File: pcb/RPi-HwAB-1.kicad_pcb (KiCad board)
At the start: 2 copper layers, 65 x 56 mm, 13 parts, among them J1 GPIO, J2 Hirose_FH12-16S, J3 TC2030, J4 Conn_ARM_SWD_TagConnect_TC203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, U1 XC7A35T-FGG484, U2 CAT24C256, U3 ADP5054

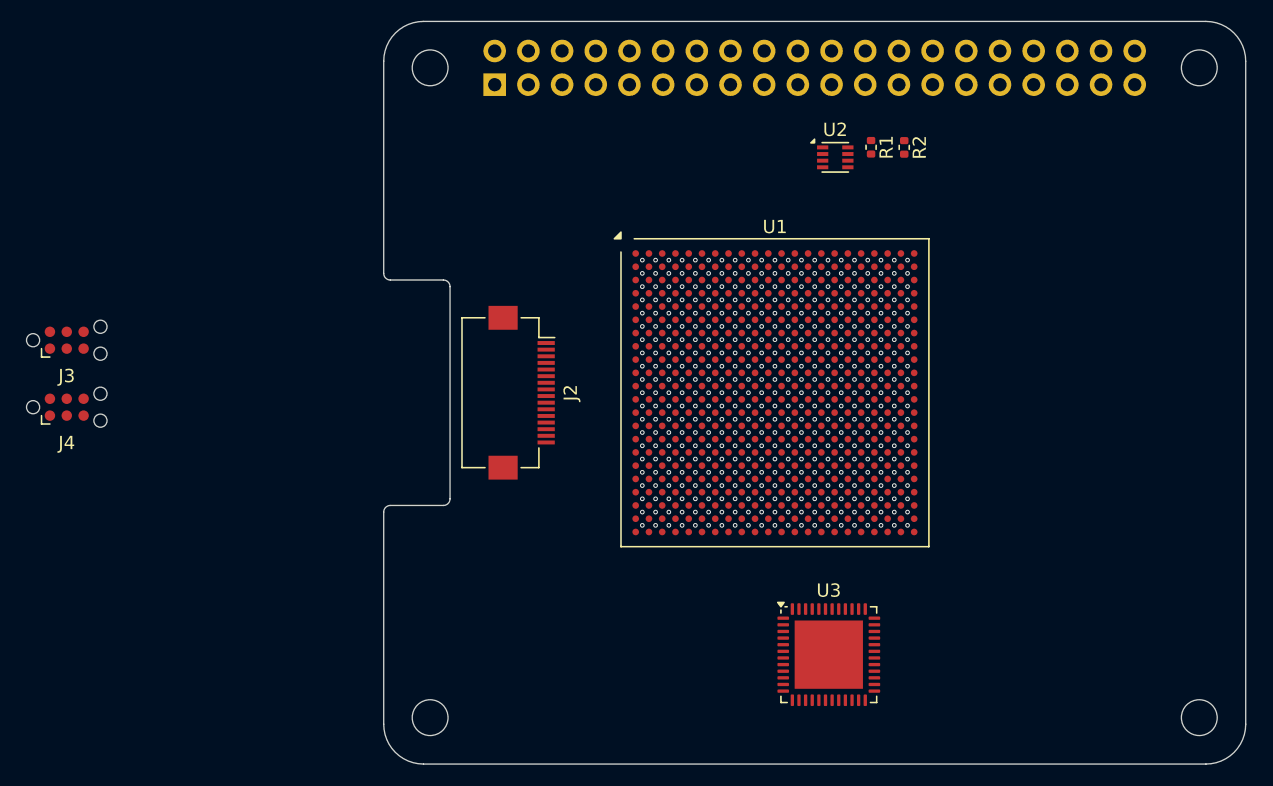
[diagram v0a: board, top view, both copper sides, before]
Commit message: addl. updates to power hierarchy
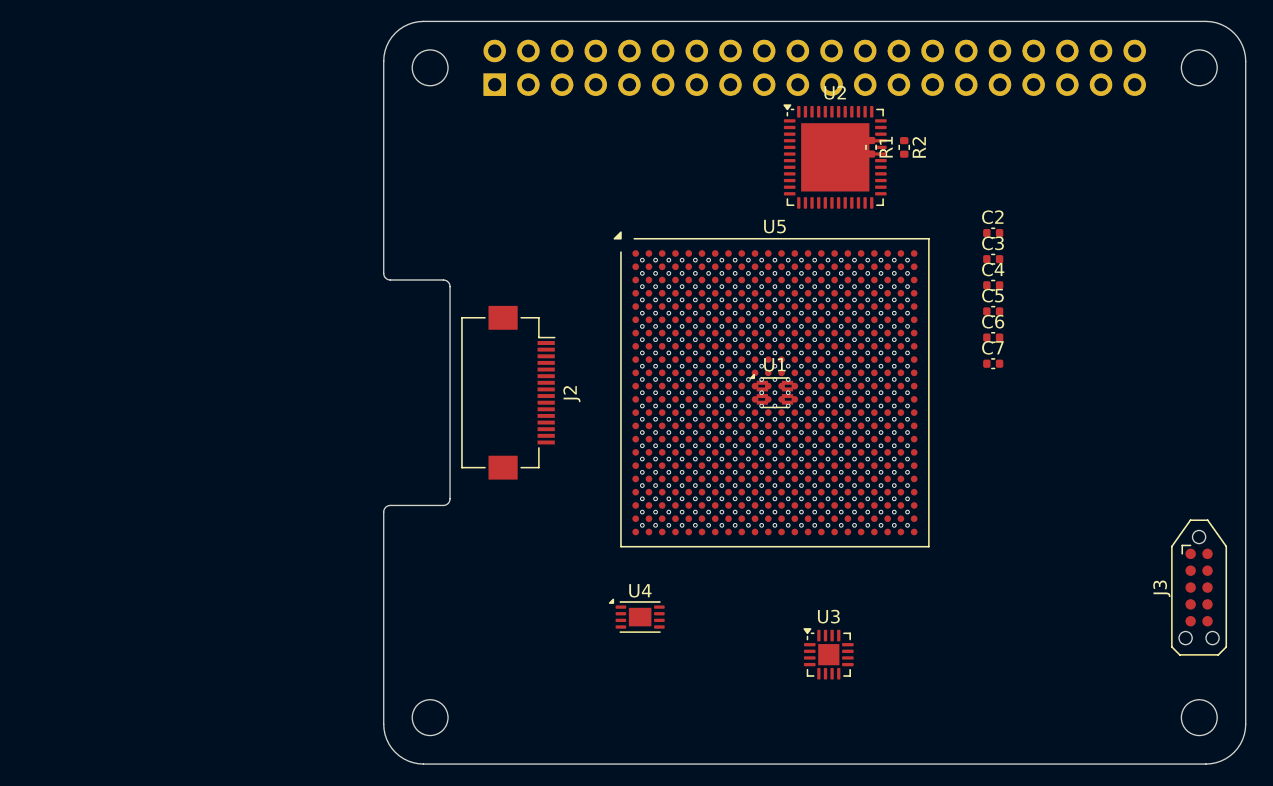
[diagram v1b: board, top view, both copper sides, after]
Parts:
- removed J4: Conn_ARM_SWD_TagConnect_TC2030-NL, Connector:Tag-Connect_TC2030-IDC-NL_2x03_P1.27mm_Vertical
- added C2: 0.1uF, Capacitor_SMD:C_0402_1005Metric, F.Cu at (146.0, 60.0)
- added C3: 0.1uF, Capacitor_SMD:C_0402_1005Metric, F.Cu at (146.0, 61.9)
- added C4: 0.1uF, Capacitor_SMD:C_0402_1005Metric, F.Cu at (146.0, 63.9)
- added C5: 0.1uF, Capacitor_SMD:C_0402_1005Metric, F.Cu at (146.0, 65.9)
- added C6: 0.1uF, Capacitor_SMD:C_0402_1005Metric, F.Cu at (146.0, 67.8)
- added C7: 0.1uF, Capacitor_SMD:C_0402_1005Metric, F.Cu at (146.0, 69.8)
- added U4: MCP9804_DFN, Package_DFN_QFN:DFN-8-1EP_3x2mm_P0.5mm_EP1.7x1.4mm, F.Cu at (119.3, 88.9)
- added U5: XC7A35T-FGG484, Package_BGA:Xilinx_FGG484, F.Cu at (129.5, 72.0)
- J3: value TC2030 -> TC2050; footprint Connector:Tag-Connect_TC2030-IDC-NL_2x03_P1.27mm_Vertical -> Connector:Tag-Connect_TC2050-IDC-NL_2x05_P1.27mm_Vertical
- U1: value XC7A35T-FGG484 -> CAT24C256; footprint Package_BGA:Xilinx_FGG484 -> Package_DFN_QFN:DFN-8_2x2mm_P0.5mm
- U2: value CAT24C256 -> ADP5054; footprint Package_DFN_QFN:DFN-8_2x2mm_P0.5mm -> Package_DFN_QFN:QFN-48-1EP_7x7mm_P0.5mm_EP5.15x5.15mm
- U3: value ADP5054 -> INA230AIRGTT; footprint Package_DFN_QFN:QFN-48-1EP_7x7mm_P0.5mm_EP5.15x5.15mm -> Package_DFN_QFN:VQFN-16-1EP_3x3mm_P0.5mm_EP1.6x1.6mm
- moved J3 87.4 mm to (161.5, 86.7), turned to -90 degrees
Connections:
- net +5V renamed +5V0
- J3 pad 2: /SWDIO -> unconnected-(J3-Pad2)
- J3 pad 3: /nRESET -> unconnected-(J3-Pad3)
- J3 pad 4: /SWCLK -> unconnected-(J3-Pad4)
- J3 pad 5: GND -> unconnected-(J3-Pad5)
- J3 pad 6: /SWO -> unconnected-(J3-Pad6)
- U2 pad 2: unconnected-(U2-A1-Pad2) -> Net-(U2-PGND3-Pad2)
- U2 pad 3: unconnected-(U2-A2-Pad3) -> Net-(U2-PGND3-Pad2)
- U2 pad 4: GND -> Net-(U2-SW3-Pad4)
- U2 pad 5: /ID_SDA -> Net-(U2-SW3-Pad4)
- U2 pad 6: /ID_SCL -> unconnected-(U2-PVIN3-Pad6)
- U2 pad 7: Net-(JP1-A) -> unconnected-(U2-PVIN4-Pad7)
- U2 pad 8: +3V3 -> Net-(U2-SW4-Pad8)
- U3 pad 10: Net-(U3-PGND4-Pad10) -> unconnected-(U3-GND-Pad10)
- U3 pad 11: Net-(U3-PGND4-Pad10) -> unconnected-(U3-BUS-Pad11)
- U3 pad 2: Net-(U3-PGND3-Pad2) -> unconnected-(U3-A0-Pad2)
- U3 pad 3: Net-(U3-PGND3-Pad2) -> unconnected-(U3-ALERT-Pad3)
- U3 pad 4: Net-(U3-SW3-Pad4) -> unconnected-(U3-SDA-Pad4)
- U3 pad 5: Net-(U3-SW3-Pad4) -> unconnected-(U3-SCL-Pad5)
- U3 pad 8: Net-(U3-SW4-Pad8) -> unconnected-(U3-NC-Pad8)
- U3 pad 9: Net-(U3-SW4-Pad8) -> (no net)
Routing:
- net unconnected-(U1-A0-Pad1): vias 0 -> 1
- net GND: vias 0 -> 1
- net /ID_SDA: vias 0 -> 1
- net +3V3: vias 0 -> 1
- net (no net): vias 441 -> 437
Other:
- copper layers 2 -> 6

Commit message: quick edits to hierarchy
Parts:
- added 1V0: TestPoint, TestPoint:TestPoint_Pad_D1.0mm, B.Cu at (154.7, 66.4)
- added 1V8: TestPoint, TestPoint:TestPoint_Pad_D1.0mm, B.Cu at (154.7, 69.4)
- added 2V5: TestPoint, TestPoint:TestPoint_Pad_D1.0mm, B.Cu at (154.7, 72.5)
- added C1: 100n, Capacitor_SMD:C_0402_1005Metric, F.Cu at (115.0, 57.5)
- added JP1: ID_WP, Jumper:SolderJumper-2_P1.3mm_Open_Pad1.0x1.5mm, F.Cu at (115.8, 54.7)
- added M1V0: TestPoint, TestPoint:TestPoint_Pad_D1.0mm, B.Cu at (154.7, 75.5)
- added M1V2: TestPoint, TestPoint:TestPoint_Pad_D1.0mm, B.Cu at (154.7, 78.6)
- added U6: INA230AIRGTT, Package_DFN_QFN:VQFN-16-1EP_3x3mm_P0.5mm_EP1.6x1.6mm, F.Cu at (148.6, 67.5)
- added U7: INA230AIRGTT, Package_DFN_QFN:VQFN-16-1EP_3x3mm_P0.5mm_EP1.6x1.6mm, F.Cu at (148.6, 72.8)
- J2: footprint Connector_FFC-FPC:Hirose_FH12-16S-0.5SH_1x16-1MP_P0.50mm_Horizontal -> Connector_FFC-FPC:Hirose_FH12-17S-0.5SH_1x17-1MP_P0.50mm_Horizontal
- moved U2 4.16 mm to (130.2, 55.9), turned to 180 degrees
- moved J2 0.45 mm to (110.0, 72.0)
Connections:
- J1 pad 3: /GPIO2/SDA1 -> /SDA1
- J1 pad 5: /GPIO3/SCL1 -> /SCL1
- J2 pad 10: /PCIE_TX_P -> /PCIE_RX_P
- J2 pad 11: /PCIE_TX_N -> /PCIE_RX_N
- J2 pad 7: /PCIE_RX_P -> /PCIE_TX_P
- J2 pad 8: /PCIE_RX_N -> /PCIE_TX_N
- U2 pad 14: unconnected-(U2-EN4-Pad14) -> /GPIO17
- U2 pad 17: unconnected-(U2-PWRGD-Pad17) -> /GPIO12/PWM0
- U2 pad 21: unconnected-(U2-EN2-Pad21) -> /GPIO15/RXD0
- U2 pad 39: unconnected-(U2-EN1-Pad39) -> /GPIO14/TXD0
- U2 pad 48: unconnected-(U2-EN3-Pad48) -> /GPIO16
- U3 pad 4: unconnected-(U3-SDA-Pad4) -> /SDA1
- U3 pad 5: unconnected-(U3-SCL-Pad5) -> /SCL1

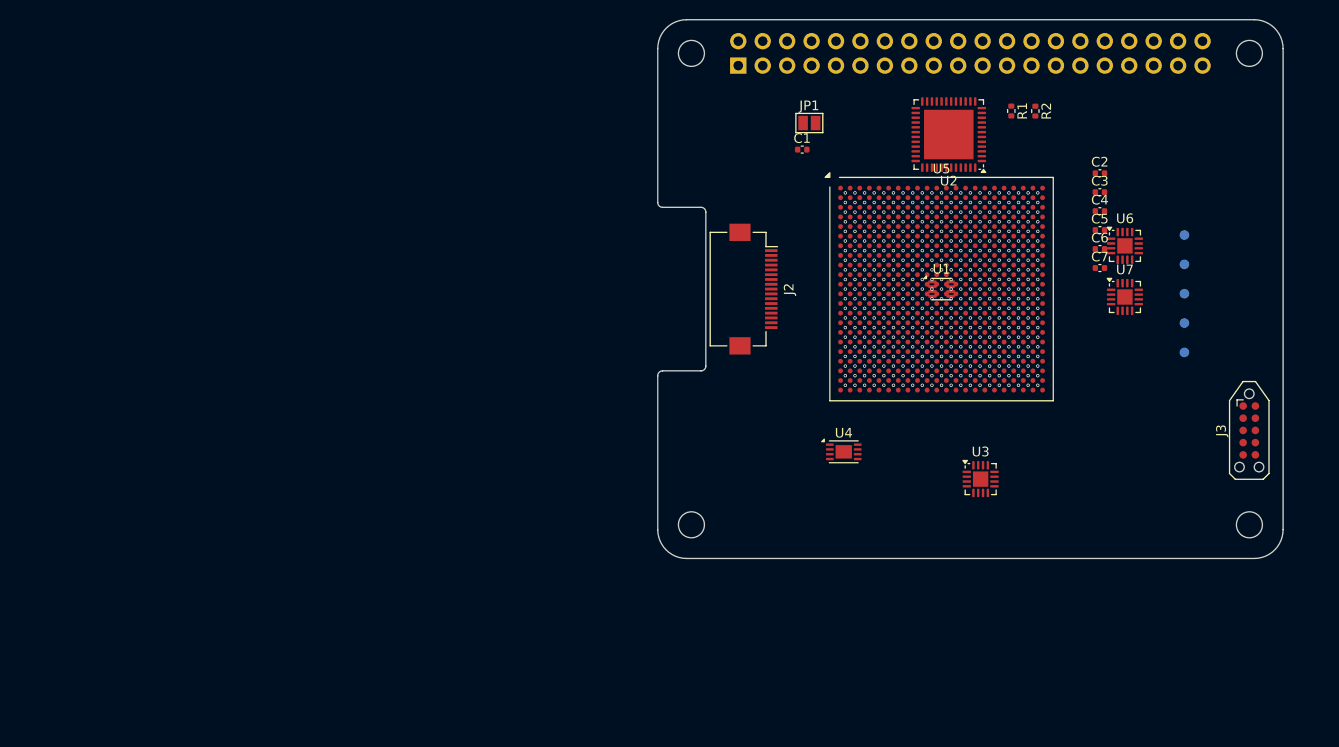
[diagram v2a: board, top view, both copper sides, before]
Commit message: changed spi flash to wson
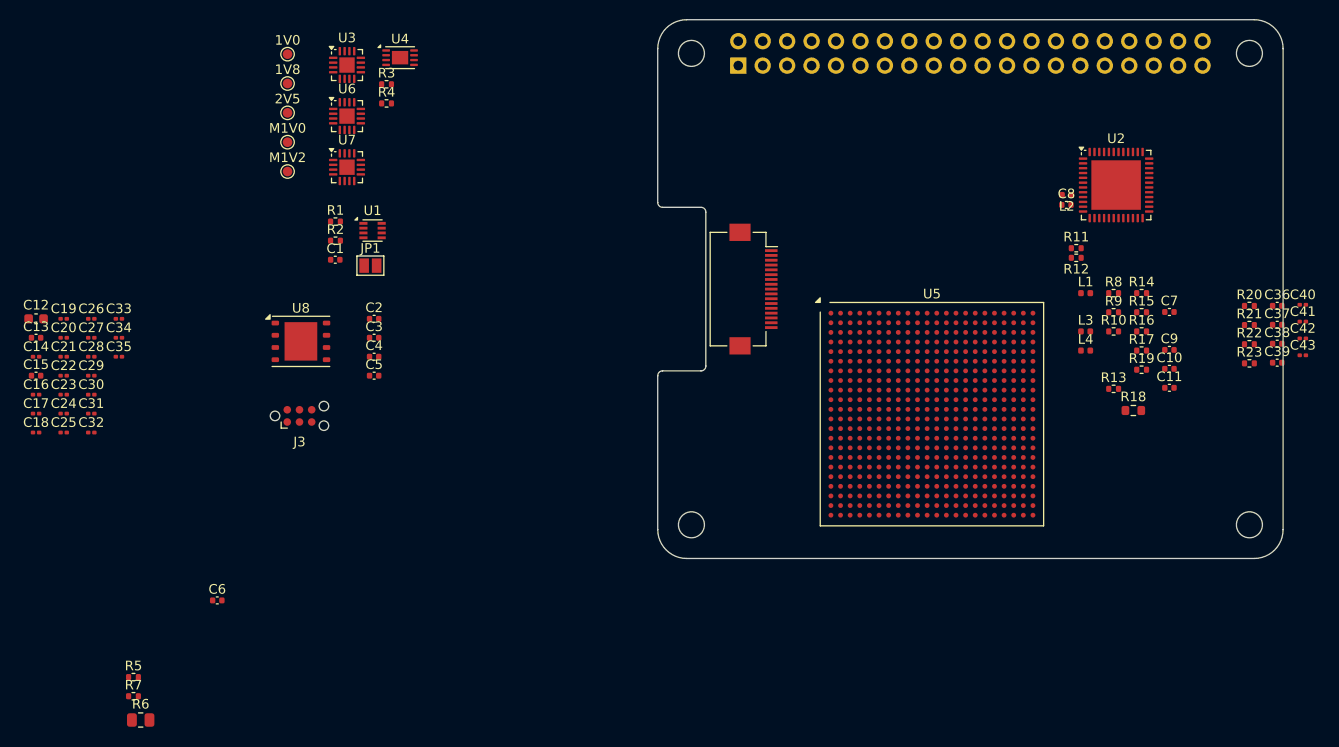
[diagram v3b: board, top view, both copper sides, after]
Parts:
- added C10: 0.1uF, Capacitor_SMD:C_0402_1005Metric, F.Cu at (153.2, 80.3)
- added C11: 0.1uF, Capacitor_SMD:C_0402_1005Metric, F.Cu at (153.2, 82.3)
- added C12: 47uF, Capacitor_SMD:C_0603_1608Metric, F.Cu at (35.4, 75.1)
- added C13: 0.1uF, Capacitor_SMD:C_0402_1005Metric, F.Cu at (35.4, 77.1)
- added C14: 0.1uF, Capacitor_SMD:C_0201_0603Metric, F.Cu at (35.4, 79.0)
- added C15: 10uF, Capacitor_SMD:C_0402_1005Metric, F.Cu at (35.4, 81.0)
- added C16: 0.1uF, Capacitor_SMD:C_0201_0603Metric, F.Cu at (35.4, 83.0)
- added C17: 0.1uF, Capacitor_SMD:C_0201_0603Metric, F.Cu at (35.4, 84.9)
- added C18: 0.1uF, Capacitor_SMD:C_0201_0603Metric, F.Cu at (35.4, 86.9)
- added C19: 0.1uF, Capacitor_SMD:C_0201_0603Metric, F.Cu at (38.2, 75.1)
- added C20: 0.1uF, Capacitor_SMD:C_0201_0603Metric, F.Cu at (38.2, 77.1)
- added C21: 0.1uF, Capacitor_SMD:C_0201_0603Metric, F.Cu at (38.2, 79.0)
- added C22: 0.1uF, Capacitor_SMD:C_0201_0603Metric, F.Cu at (38.2, 81.0)
- added C23: 0.1uF, Capacitor_SMD:C_0201_0603Metric, F.Cu at (38.2, 83.0)
- added C24: 0.1uF, Capacitor_SMD:C_0201_0603Metric, F.Cu at (38.2, 84.9)
- added C25: 0.1uF, Capacitor_SMD:C_0201_0603Metric, F.Cu at (38.2, 86.9)
- added C26: 0.1uF, Capacitor_SMD:C_0201_0603Metric, F.Cu at (41.1, 75.1)
- added C27: 0.1uF, Capacitor_SMD:C_0201_0603Metric, F.Cu at (41.1, 77.1)
- added C28: 0.1uF, Capacitor_SMD:C_0201_0603Metric, F.Cu at (41.1, 79.0)
- added C29: 0.1uF, Capacitor_SMD:C_0201_0603Metric, F.Cu at (41.1, 81.0)
- added C30: 0.1uF, Capacitor_SMD:C_0201_0603Metric, F.Cu at (41.1, 83.0)
- added C31: 0.1uF, Capacitor_SMD:C_0201_0603Metric, F.Cu at (41.1, 84.9)
- added C32: 0.1uF, Capacitor_SMD:C_0201_0603Metric, F.Cu at (41.1, 86.9)
- added C33: 0.1uF, Capacitor_SMD:C_0201_0603Metric, F.Cu at (44.0, 75.1)
- added C34: 0.1uF, Capacitor_SMD:C_0201_0603Metric, F.Cu at (44.0, 77.1)
- added C35: 0.1uF, Capacitor_SMD:C_0201_0603Metric, F.Cu at (44.0, 79.0)
- added C36: 10uF, Capacitor_SMD:C_0402_1005Metric, F.Cu at (164.4, 73.7)
- added C37: 10uF, Capacitor_SMD:C_0402_1005Metric, F.Cu at (164.4, 75.7)
- added C38: 10uF, Capacitor_SMD:C_0402_1005Metric, F.Cu at (164.4, 77.7)
- added C39: 10uF, Capacitor_SMD:C_0402_1005Metric, F.Cu at (164.4, 79.7)
- added C40: 2.2nF, Capacitor_SMD:C_0201_0603Metric, F.Cu at (167.1, 73.6)
- added C41: 2.2nF, Capacitor_SMD:C_0201_0603Metric, F.Cu at (167.1, 75.4)
- added C42: 2.2nF, Capacitor_SMD:C_0201_0603Metric, F.Cu at (167.1, 77.1)
- added C43: 2.2nF, Capacitor_SMD:C_0201_0603Metric, F.Cu at (167.1, 78.9)
- added C8: 0.1uF, Capacitor_SMD:C_0402_1005Metric, F.Cu at (142.5, 63.2)
- added C9: 0.1uF, Capacitor_SMD:C_0402_1005Metric, F.Cu at (153.2, 78.3)
- added L1: 1uH, Inductor_SMD:L_0402_1005Metric, F.Cu at (144.5, 72.4)
- added L2: 1uH, Inductor_SMD:L_0402_1005Metric, F.Cu at (142.5, 62.2)
- added L3: 1uH, Inductor_SMD:L_0402_1005Metric, F.Cu at (144.5, 76.4)
- added L4: 1uH, Inductor_SMD:L_0402_1005Metric, F.Cu at (144.5, 78.4)
- added R10: 24K, Resistor_SMD:R_0402_1005Metric, F.Cu at (147.4, 76.4)
- added R11: 75K, Resistor_SMD:R_0402_1005Metric, F.Cu at (143.5, 67.8)
- added R12: 24K, Resistor_SMD:R_0402_1005Metric, F.Cu at (143.5, 68.8)
- added R13: 30K, Resistor_SMD:R_0402_1005Metric, F.Cu at (147.4, 82.4)
- added R14: 120K, Resistor_SMD:R_0402_1005Metric, F.Cu at (150.3, 72.4)
- added R15: 15K, Resistor_SMD:R_0402_1005Metric, F.Cu at (150.3, 74.4)
- added R16: 30K, Resistor_SMD:R_0402_1005Metric, F.Cu at (150.3, 76.4)
- added R17: 100, Resistor_SMD:R_0402_1005Metric, F.Cu at (150.3, 78.4)
- added R18: 0.005, Resistor_SMD:R_0603_1608Metric, F.Cu at (149.4, 84.6)
- added R19: 100, Resistor_SMD:R_0402_1005Metric, F.Cu at (150.3, 80.4)
- added R20: 10K, Resistor_SMD:R_0402_1005Metric, F.Cu at (161.5, 73.8)
- added R21: 10K, Resistor_SMD:R_0402_1005Metric, F.Cu at (161.5, 75.7)
- added R22: 10K, Resistor_SMD:R_0402_1005Metric, F.Cu at (161.5, 77.7)
- added R23: 10K, Resistor_SMD:R_0402_1005Metric, F.Cu at (161.5, 79.7)
- added R3: 4.7K, Resistor_SMD:R_0402_1005Metric, F.Cu at (71.8, 50.7)
- added R4: 4.7K, Resistor_SMD:R_0402_1005Metric, F.Cu at (71.8, 52.7)
- added R5: 100, Resistor_SMD:R_0402_1005Metric, F.Cu at (45.5, 112.3)
- added R6: 0.003, Resistor_SMD:R_0805_2012Metric, F.Cu at (46.3, 116.8)
- added R7: 100, Resistor_SMD:R_0402_1005Metric, F.Cu at (45.5, 114.3)
- added R8: 31.6K, Resistor_SMD:R_0402_1005Metric, F.Cu at (147.4, 72.4)
- added R9: 30K, Resistor_SMD:R_0402_1005Metric, F.Cu at (147.4, 74.4)
- added U8: MX25L3233FZN, Package_SON:WSON-8-1EP_6x5mm_P1.27mm_EP3.4x4mm, F.Cu at (62.9, 77.4)
- 1V0, 1V8, 2V5, M1V0, M1V2: moved to F.Cu
- J3: value TC2050 -> TC2030; footprint Connector:Tag-Connect_TC2050-IDC-NL_2x05_P1.27mm_Vertical -> Connector:Tag-Connect_TC2030-IDC-NL_2x03_P1.27mm_Vertical
- moved C6 98.7 mm to (54.2, 104.4)
- moved J3 98.7 mm to (62.8, 85.2), turned to 0 degrees
- moved 1V0 95.1 mm to (61.5, 47.6), turned to 0 degrees
- moved 1V8 95.1 mm to (61.5, 50.6), turned to 0 degrees
- moved 2V5 95.1 mm to (61.5, 53.7), turned to 0 degrees
- moved M1V0 95.1 mm to (61.5, 56.7), turned to 0 degrees
- moved M1V2 95.1 mm to (61.5, 59.8), turned to 0 degrees
- moved U6 82.0 mm to (67.7, 54.0)
- moved U7 82.0 mm to (67.7, 59.3)
- moved U3 78.7 mm to (67.7, 48.7)
- moved C2 76.9 mm to (70.5, 75.1)
- moved C3 76.9 mm to (70.5, 77.1)
- moved C4 76.9 mm to (70.5, 79.0)
- moved C5 76.9 mm to (70.5, 81.0)
- moved R2 74.0 mm to (66.5, 67.0), turned to 0 degrees
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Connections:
- net +1V2_MGT renamed /FPGA/1V2_MGT
- net +1V8_FD renamed /FPGA/1V8_FD
- net +5V0 renamed /Connectors/5V0
- net /GPIO14/TXD0 renamed /Connectors/EN1
- net /GPIO15/RXD0 renamed /Connectors/EN2
- net /GPIO7/SPI0.CE1 renamed /Connectors/SPI0.CS1
- net /PCIE_CLKREQ_N renamed /Connectors/PCIE.CLKREQ_N
- net /PCIE_CLK_N renamed /Connectors/PCIE.CLK_N
- net /PCIE_CLK_P renamed /Connectors/PCIE.CLK_P
- net /PCIE_DET_WAKE renamed /Connectors/PCIE.DET_WAKE
- net /PCIE_PWR_EN renamed /Connectors/PCIE.PWR_EN
- net /PCIE_RST_B renamed /Connectors/PCIE.RST_B
- net /PCIE_RX_N renamed /Connectors/PCIE.P2F_N
- net /PCIE_RX_P renamed /Connectors/PCIE.P2F_P
- net /PCIE_TX_N renamed /Connectors/PCIE.F2P_N
- net /PCIE_TX_P renamed /Connectors/PCIE.F2P_P
- net /SCL1 renamed /Connectors/I2C1.SCL
- net Net-(U2-SW3-Pad4) renamed /Main Power/SW3
- net Net-(U2-SW4-Pad8) renamed /Main Power/SW4
- 1V0 pad 1: +1V0_FD -> /FPGA/1V0_FD
- 2V5 pad 1: +2V5_FD -> /FPGA/FPGA Power/2V5_FD
- C2 pad 1: unconnected-(C2-Pad1) -> Net-(U5F-MGTPTXN0_216)
- C2 pad 2: unconnected-(C2-Pad2) -> /FPGA/FPGA 3/PCIE.TX_N
- C3 pad 1: unconnected-(C3-Pad1) -> Net-(U5F-MGTPRXN0_216)
- C3 pad 2: unconnected-(C3-Pad2) -> /FPGA/FPGA 3/PCIE.RX_N
- C4 pad 1: unconnected-(C4-Pad1) -> Net-(U5F-MGTPTXP0_216)
- C4 pad 2: unconnected-(C4-Pad2) -> /FPGA/FPGA 3/PCIE.TX_P
- C5 pad 1: unconnected-(C5-Pad1) -> Net-(U5F-MGTPRXP0_216)
- C5 pad 2: unconnected-(C5-Pad2) -> /FPGA/FPGA 3/PCIE.RX_P
- C6 pad 1: unconnected-(C6-Pad1) -> /Main Power/5V0_SENS_P
- C6 pad 2: unconnected-(C6-Pad2) -> /Main Power/5V0_SENS_N
- C7 pad 1: unconnected-(C7-Pad1) -> /Main Power/BST2
- C7 pad 2: unconnected-(C7-Pad2) -> /Main Power/SW2
- J1 pad 1: +3V3 -> /Connectors/3V3
- J1 pad 11: /GPIO17 -> unconnected-(J1-Pin_11-Pad11)
- J1 pad 12: /GPIO18/PCM.CLK -> /Connectors/EN3
- J1 pad 13: /GPIO27 -> unconnected-(J1-Pin_13-Pad13)
- J1 pad 15: /GPIO22 -> unconnected-(J1-Pin_15-Pad15)
- J1 pad 16: /GPIO23 -> /Connectors/EN4
- J1 pad 17: +3V3 -> /Connectors/3V3
- J1 pad 18: /GPIO24 -> /Connectors/PGOOD
- J1 pad 19: /GPIO10/SPI0.MOSI -> /Connectors/SPI0.MOSI
- J1 pad 21: /GPIO9/SPI0.MISO -> /Connectors/SPI0.MISO
- J1 pad 22: /GPIO25 -> unconnected-(J1-Pin_22-Pad22)
- J1 pad 23: /GPIO11/SPI0.SCLK -> /Connectors/SPI0.SCK
- J1 pad 24: /GPIO8/SPI0.CE0 -> /Connectors/SPI0.CS0
- J1 pad 27: /ID_SDA -> /Connectors/ID_SDA
- J1 pad 28: /ID_SCL -> /Connectors/ID_SCL
- J1 pad 29: /GPIO5 -> unconnected-(J1-Pin_29-Pad29)
- J1 pad 3: /SDA1 -> /Connectors/I2C1.SDA
- J1 pad 31: /GPIO6 -> unconnected-(J1-Pin_31-Pad31)
- J1 pad 32: /GPIO12/PWM0 -> unconnected-(J1-Pin_32-Pad32)
- J1 pad 33: /GPIO13/PWM1 -> unconnected-(J1-Pin_33-Pad33)
- J1 pad 35: /GPIO19/PCM.FS -> unconnected-(J1-Pin_35-Pad35)
- J1 pad 36: /GPIO16 -> unconnected-(J1-Pin_36-Pad36)
- J1 pad 37: /GPIO26 -> unconnected-(J1-Pin_37-Pad37)
- J1 pad 38: /GPIO20/PCM.DIN -> unconnected-(J1-Pin_38-Pad38)
- J1 pad 40: /GPIO21/PCM.DOUT -> unconnected-(J1-Pin_40-Pad40)
- J1 pad 7: /GPIO4/GPCLK0 -> unconnected-(J1-Pin_7-Pad7)
- J3 pad 1: unconnected-(J3-Pad1) -> /Connectors/3V3
- J3 pad 2: unconnected-(J3-Pad2) -> /Connectors/TMS
- J3 pad 3: unconnected-(J3-Pad3) -> /Connectors/TDI
- J3 pad 4: unconnected-(J3-Pad4) -> /Connectors/TCK
- J3 pad 5: unconnected-(J3-Pad5) -> GND
- J3 pad 6: unconnected-(J3-Pad6) -> /Connectors/TDO
- M1V0 pad 1: +1V0_MGT -> /FPGA/1V0_FD
- U2 pad 1: unconnected-(U2-BST3-Pad1) -> /Main Power/BST3
- U2 pad 10: Net-(U2-PGND4-Pad10) -> GND
- U2 pad 11: Net-(U2-PGND4-Pad10) -> GND
- U2 pad 12: unconnected-(U2-BST4-Pad12) -> /Main Power/BST4
- U2 pad 14: /GPIO17 -> /Connectors/EN4
- U2 pad 15: unconnected-(U2-COMP4-Pad15) -> /Main Power/Comp & Decpl./COMP4
- U2 pad 16: unconnected-(U2-FB4-Pad16) -> /Main Power/FB4
- U2 pad 17: /GPIO12/PWM0 -> /Connectors/PGOOD
- U2 pad 19: unconnected-(U2-FB2-Pad19) -> /Main Power/FB2
- U2 pad 2: Net-(U2-PGND3-Pad2) -> GND
- U2 pad 20: unconnected-(U2-COMP2-Pad20) -> /Main Power/Comp & Decpl./COMP2
- U2 pad 22: Net-(U2-PVIN2-Pad22) -> /Main Power/5V0_N
- U2 pad 23: Net-(U2-PVIN2-Pad22) -> /Main Power/5V0_N
- U2 pad 24: Net-(U2-PVIN2-Pad22) -> /Main Power/5V0_N
- U2 pad 25: Net-(U2-SW2-Pad25) -> /Main Power/SW2
- U2 pad 26: Net-(U2-SW2-Pad25) -> /Main Power/SW2
- U2 pad 27: Net-(U2-SW2-Pad25) -> /Main Power/SW2
- U2 pad 28: unconnected-(U2-BST2-Pad28) -> /Main Power/BST2
- U2 pad 3: Net-(U2-PGND3-Pad2) -> GND
- U2 pad 30: unconnected-(U2-PGND-Pad30) -> GND
- U2 pad 32: unconnected-(U2-BST1-Pad32) -> /Main Power/BST1
- U2 pad 33: Net-(U2-SW1-Pad33) -> /Main Power/FB1
- U2 pad 34: Net-(U2-SW1-Pad33) -> /Main Power/FB1
- U2 pad 35: Net-(U2-SW1-Pad33) -> /Main Power/SW1
- U2 pad 36: Net-(U2-PVIN1-Pad36) -> /Main Power/5V0_N
- U2 pad 37: Net-(U2-PVIN1-Pad36) -> /Main Power/5V0_N
- U2 pad 38: Net-(U2-PVIN1-Pad36) -> /Main Power/5V0_N
- U2 pad 40: unconnected-(U2-COMP1-Pad40) -> /Main Power/Comp & Decpl./COMP1
- U2 pad 41: unconnected-(U2-FB1-Pad41) -> /Main Power/FB1
- U2 pad 42: unconnected-(U2-RT-Pad42) -> Net-(U2-RT)
- U2 pad 44: unconnected-(U2-SYNC/MODE-Pad44) -> GND
- U2 pad 46: unconnected-(U2-FB3-Pad46) -> /Main Power/FB3
- U2 pad 47: unconnected-(U2-COMP3-Pad47) -> /Main Power/Comp & Decpl./COMP3
- U2 pad 48: /GPIO16 -> /Connectors/EN3
- U2 pad 49: unconnected-(U2-EPAD-Pad49) -> GND
- U2 pad 6: unconnected-(U2-PVIN3-Pad6) -> /Main Power/5V0_N
- U2 pad 7: unconnected-(U2-PVIN4-Pad7) -> /Main Power/5V0_N
- U3 pad 1: unconnected-(U3-A1-Pad1) -> GND
- U3 pad 10: unconnected-(U3-GND-Pad10) -> GND
- U3 pad 11: unconnected-(U3-BUS-Pad11) -> /Main Power/5V0_SENS_N
- U3 pad 12: unconnected-(U3-IN--Pad12) -> /Main Power/5V0_SENS_P
- U3 pad 13: unconnected-(U3-IN+-Pad13) -> /Main Power/5V0_SENS_N
- U3 pad 17: unconnected-(U3-E-PAD-Pad17) -> GND
- U3 pad 2: unconnected-(U3-A0-Pad2) -> GND
- U3 pad 4: /SDA1 -> /Connectors/I2C1.SDA
- U3 pad 6: unconnected-(U3-NC-Pad6) -> GND
- U3 pad 7: unconnected-(U3-NC-Pad7) -> GND
- U3 pad 8: unconnected-(U3-NC-Pad8) -> /Connectors/3V3
- U5 pad A17: +2V5_FD -> /FPGA/3V3_FD
- U5 pad A4: unconnected-(U5F-MGTPTXN0_216-PadA4) -> Net-(U5F-MGTPTXN0_216)
- U5 pad A8: unconnected-(U5F-MGTPRXN0_216-PadA8) -> Net-(U5F-MGTPRXN0_216)
- U5 pad AA17: +2V5_FD -> /FPGA/3V3_FD
- U5 pad AA7: +2V5_FD -> /FPGA/3V3_FD
- U5 pad AB14: +2V5_FD -> /FPGA/3V3_FD
- U5 pad AB4: +2V5_FD -> /FPGA/3V3_FD
- U5 pad B14: +2V5_FD -> /FPGA/3V3_FD
- U5 pad B4: unconnected-(U5F-MGTPTXP0_216-PadB4) -> Net-(U5F-MGTPTXP0_216)
- U5 pad B8: unconnected-(U5F-MGTPRXP0_216-PadB8) -> Net-(U5F-MGTPRXP0_216)
- U5 pad C1: +2V5_FD -> /FPGA/3V3_FD
- U5 pad C21: +2V5_FD -> /FPGA/3V3_FD
- U5 pad D10: +1V0_MGT -> /FPGA/1V0_FD
- U5 pad D18: +2V5_FD -> /FPGA/3V3_FD
- U5 pad D6: +1V0_MGT -> /FPGA/1V0_FD
- U5 pad E15: +2V5_FD -> /FPGA/3V3_FD
- U5 pad E6: unconnected-(U5F-MGTREFCLK0N_216-PadE6) -> /FPGA/FPGA 3/PCIE.CLK_N
- U5 pad E8: +1V0_MGT -> /FPGA/1V0_FD
- U5 pad F12: +2V5_FD -> /FPGA/3V3_FD
- U5 pad F2: +2V5_FD -> /FPGA/3V3_FD
- U5 pad F22: +2V5_FD -> /FPGA/3V3_FD
- U5 pad F6: unconnected-(U5F-MGTREFCLK0P_216-PadF6) -> /FPGA/FPGA 3/PCIE.CLK_P
- U5 pad F7: +1V0_MGT -> /FPGA/1V0_FD
- U5 pad F9: +1V0_MGT -> /FPGA/1V0_FD
- U5 pad G19: +2V5_FD -> /FPGA/3V3_FD
- U5 pad H10: +1V0_FD -> /FPGA/1V0_FD
- U5 pad H16: +2V5_FD -> /FPGA/3V3_FD
- U5 pad H6: +2V5_FD -> /FPGA/3V3_FD
- U5 pad H8: +1V0_FD -> /FPGA/1V0_FD
- U5 pad J11: +1V0_FD -> /FPGA/1V0_FD
- U5 pad J13: +2V5_FD -> /FPGA/3V3_FD
- U5 pad J3: +2V5_FD -> /FPGA/3V3_FD
- U5 pad J7: +1V0_FD -> /FPGA/1V0_FD
- U5 pad J9: +1V0_FD -> /FPGA/1V0_FD
- U5 pad K20: +2V5_FD -> /FPGA/3V3_FD
- U5 pad K8: +1V0_FD -> /FPGA/1V0_FD
- U5 pad L11: +1V0_FD -> /FPGA/1V0_FD
- U5 pad L17: +2V5_FD -> /FPGA/3V3_FD
- U5 pad L7: +1V0_FD -> /FPGA/1V0_FD
- U5 pad M14: +2V5_FD -> /FPGA/3V3_FD
- U5 pad M4: +2V5_FD -> /FPGA/3V3_FD
- U5 pad M8: +1V0_FD -> /FPGA/1V0_FD
- U5 pad N1: +2V5_FD -> /FPGA/3V3_FD
- U5 pad N11: +1V0_FD -> /FPGA/1V0_FD
- U5 pad N21: +2V5_FD -> /FPGA/3V3_FD
- U5 pad N7: +1V0_FD -> /FPGA/1V0_FD
- U5 pad P10: +1V0_FD -> /FPGA/1V0_FD
- U5 pad P18: +2V5_FD -> /FPGA/3V3_FD
- U5 pad P8: +1V0_FD -> /FPGA/1V0_FD
- U5 pad R13: unconnected-(U5H-TDI_0-PadR13) -> /Connectors/TDI
- U5 pad R15: +2V5_FD -> /FPGA/3V3_FD
- U5 pad R5: +2V5_FD -> /FPGA/3V3_FD
- U5 pad R7: +1V0_FD -> /FPGA/1V0_FD
- U5 pad R9: +1V0_FD -> /FPGA/1V0_FD
- U5 pad T10: +1V0_FD -> /FPGA/1V0_FD
- U5 pad T12: +2V5_FD -> /FPGA/3V3_FD
- U5 pad T13: unconnected-(U5H-TMS_0-PadT13) -> /Connectors/TMS
- U5 pad T2: +2V5_FD -> /FPGA/3V3_FD
- U5 pad T22: +2V5_FD -> /FPGA/3V3_FD
- U5 pad T8: +1V0_FD -> /FPGA/1V0_FD
- U5 pad U13: unconnected-(U5H-TDO_0-PadU13) -> /Connectors/TDO
- U5 pad U19: +2V5_FD -> /FPGA/3V3_FD
- U5 pad V12: unconnected-(U5H-TCK_0-PadV12) -> /Connectors/TCK
- U5 pad V16: +2V5_FD -> /FPGA/3V3_FD
- U5 pad V6: +2V5_FD -> /FPGA/3V3_FD
- U5 pad W13: +2V5_FD -> /FPGA/3V3_FD
- U5 pad W3: +2V5_FD -> /FPGA/3V3_FD
- U5 pad Y10: +2V5_FD -> /FPGA/3V3_FD
- U5 pad Y20: +2V5_FD -> /FPGA/3V3_FD
- U6 pad 1: unconnected-(U6-A1-Pad1) -> GND
- U6 pad 10: unconnected-(U6-GND-Pad10) -> GND
- U6 pad 11: unconnected-(U6-BUS-Pad11) -> /Main Power/1V0_SENS_P
- U6 pad 12: unconnected-(U6-IN--Pad12) -> /Main Power/1V0_SENS_N
- U6 pad 13: unconnected-(U6-IN+-Pad13) -> /Main Power/1V0_SENS_P
- U6 pad 17: unconnected-(U6-E-PAD-Pad17) -> GND
- U6 pad 2: unconnected-(U6-A0-Pad2) -> /Connectors/3V3
- U6 pad 4: /SDA1 -> /Connectors/I2C1.SDA
- U6 pad 6: unconnected-(U6-NC-Pad6) -> GND
- U6 pad 7: unconnected-(U6-NC-Pad7) -> GND
- U6 pad 8: unconnected-(U6-NC-Pad8) -> /Connectors/3V3
- U7 pad 1: unconnected-(U7-A1-Pad1) -> GND
- U7 pad 10: unconnected-(U7-GND-Pad10) -> GND
- U7 pad 17: unconnected-(U7-E-PAD-Pad17) -> GND
- U7 pad 2: unconnected-(U7-A0-Pad2) -> /Connectors/I2C1.SDA
- U7 pad 4: /SDA1 -> /Connectors/I2C1.SDA
- U7 pad 6: unconnected-(U7-NC-Pad6) -> GND
- U7 pad 7: unconnected-(U7-NC-Pad7) -> GND
- U7 pad 8: unconnected-(U7-NC-Pad8) -> /Connectors/3V3
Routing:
- net unconnected-(U1-A0-Pad1): vias 1 -> 0
- net GND: vias 1 -> 0
- net /ID_SDA: vias 1 -> 0
- net +3V3: vias 1 -> 0
- net (no net): vias 437 -> 0

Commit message: pcie definitions
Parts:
- removed 2V5: TestPoint, TestPoint:TestPoint_Pad_D1.0mm
- removed C3, C5: 0.1uF, Capacitor_SMD:C_0402_1005Metric
- removed U7: INA230AIRGTT, Package_DFN_QFN:VQFN-16-1EP_3x3mm_P0.5mm_EP1.6x1.6mm
- added 3V3: TestPoint, TestPoint:TestPoint_Pad_D1.0mm, F.Cu at (28.8, 44.9)
- added C44: 10uF, Capacitor_SMD:C_0603_1608Metric, F.Cu at (39.5, 32.7)
- added C45: 47uF, Capacitor_SMD:C_0603_1608Metric, F.Cu at (39.5, 35.2)
- added C46: 47uF, Capacitor_SMD:C_0603_1608Metric, F.Cu at (39.5, 37.8)
- added C47: 10uF, Capacitor_SMD:C_0402_1005Metric, F.Cu at (28.7, 32.5)
- added C48: 10uF, Capacitor_SMD:C_0402_1005Metric, F.Cu at (28.7, 34.4)
- added C49: 0.1uF, Capacitor_SMD:C_0402_1005Metric, F.Cu at (28.7, 36.4)
- added C50: 0.1uF, Capacitor_SMD:C_0201_0603Metric, F.Cu at (31.3, 32.4)
- added C51: 0.1uF, Capacitor_SMD:C_0402_1005Metric, F.Cu at (28.7, 38.4)
- added C52: 0.1uF, Capacitor_SMD:C_0402_1005Metric, F.Cu at (28.7, 40.3)
- added C53: 0.1uF, Capacitor_SMD:C_0201_0603Metric, F.Cu at (31.3, 34.1)
- added C54: 0.1uF, Capacitor_SMD:C_0201_0603Metric, F.Cu at (31.3, 35.9)
- added C55: 0.1uF, Capacitor_SMD:C_0201_0603Metric, F.Cu at (31.3, 37.6)
- added C56: 0.1uF, Capacitor_SMD:C_0201_0603Metric, F.Cu at (31.3, 39.4)
- added C57: 0.1uF, Capacitor_SMD:C_0201_0603Metric, F.Cu at (33.8, 32.4)
- added C58: 0.1uF, Capacitor_SMD:C_0201_0603Metric, F.Cu at (33.8, 34.1)
- added C59: 0.1uF, Capacitor_SMD:C_0201_0603Metric, F.Cu at (33.8, 35.9)
- added C60: 0.1uF, Capacitor_SMD:C_0201_0603Metric, F.Cu at (33.8, 37.6)
- added C61: 0.1uF, Capacitor_SMD:C_0201_0603Metric, F.Cu at (33.8, 39.4)
- added C62: 0.1uF, Capacitor_SMD:C_0201_0603Metric, F.Cu at (36.2, 32.4)
- added C63: 0.1uF, Capacitor_SMD:C_0201_0603Metric, F.Cu at (36.2, 34.1)
- added C64: 0.1uF, Capacitor_SMD:C_0201_0603Metric, F.Cu at (36.2, 35.9)
- added C65: 0.1uF, Capacitor_SMD:C_0201_0603Metric, F.Cu at (36.2, 37.6)
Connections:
- net Net-(U5F-MGTPTXN0_216) renamed /FPGA/FPGA 3/F2P_N
- net Net-(U5F-MGTPTXP0_216) renamed /FPGA/FPGA 3/F2P_P
- C2 pad 2: /FPGA/FPGA 3/PCIE.TX_N -> /Connectors/PCIE.F2P_N
- C4 pad 2: /FPGA/FPGA 3/PCIE.TX_P -> /Connectors/PCIE.F2P_P
- U4 pad 1: unconnected-(U4-SDA-Pad1) -> /Connectors/I2C1.SDA
- U4 pad 2: unconnected-(U4-SCL-Pad2) -> /Connectors/I2C1.SCL
- U4 pad 4: unconnected-(U4-GND-Pad4) -> GND
- U4 pad 5: unconnected-(U4-A2-Pad5) -> GND
- U4 pad 6: unconnected-(U4-A1-Pad6) -> GND
- U4 pad 7: unconnected-(U4-A0-Pad7) -> GND
- U4 pad 8: unconnected-(U4-V_{DD}-Pad8) -> /Connectors/3V3
- U4 pad 9: unconnected-(U4-EP/GND-Pad9) -> GND
- U5 pad A8: Net-(U5F-MGTPRXN0_216) -> /Connectors/PCIE.P2F_N
- U5 pad B8: Net-(U5F-MGTPRXP0_216) -> /Connectors/PCIE.P2F_P
- U5 pad E6: /FPGA/FPGA 3/PCIE.CLK_N -> /Connectors/PCIE.CLK_N
- U5 pad F6: /FPGA/FPGA 3/PCIE.CLK_P -> /Connectors/PCIE.CLK_P
